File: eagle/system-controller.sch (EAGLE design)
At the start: 234 parts, among them CN1 22u, IC1 TS4100, J1 1, Q0 MOSFET-P-N-PAIR, Q1 MOSFET-P-N-PAIR, Q10 DNP/NTR4101P, Q11 DNP/NTR4101P, Q12 DNP/NTR4101P, Q13 DON3035L, Q2 MOSFET-P-N-PAIR, Q3 MOSFET-P-N-PAIR, Q4 MOSFET-P-N-PAIR, Q5 MOSFET-P-N-PAIR, Q6 MOSFET-P-N-PAIR, Q7 MOSFET-P-N-PAIR, Q9 DNP/NTR4101P, SW0 TPS25944LRVCRWQFN-20-3X4, SW1 TPS25944LRVCRWQFN-20-3X4, SW2 TPS25944LRVCRWQFN-20-3X4, SW3 TPS25944LRVCRWQFN-20-3X4, SW4 TPS25944LRVCRWQFN-20-3X4, SW5 TPS25944LRVCRWQFN-20-3X4, SW6 TPS25944LRVCRWQFN-20-3X4, SW7 TPS25944LRVCRWQFN-20-3X4, U1 MEGA128-A, X1 8 MHz CRYSTAL-ABRACON-ABM3-SMD

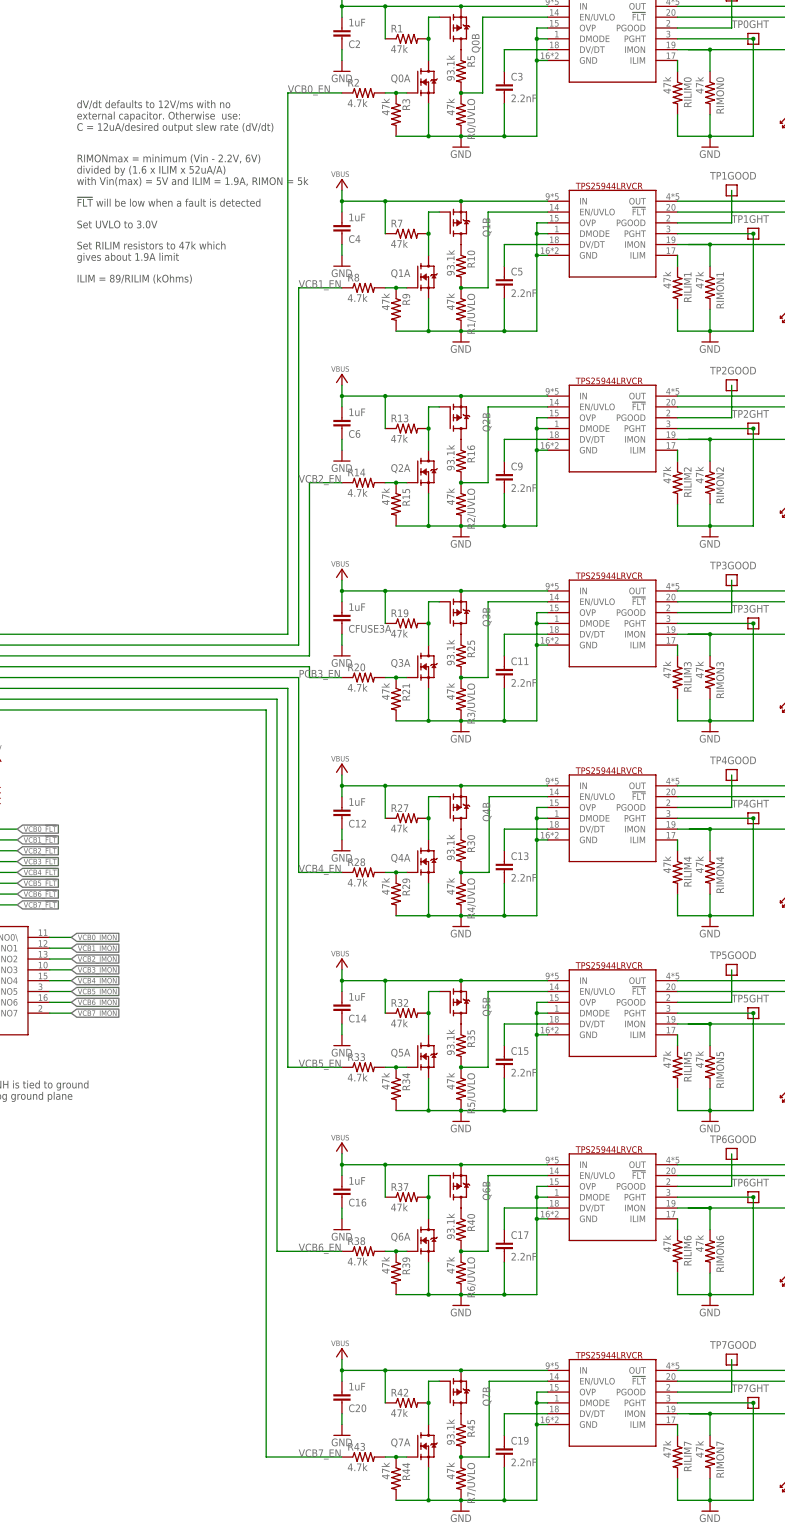
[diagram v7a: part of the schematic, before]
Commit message: made polygons wider and changed physical layout of them. Also, reduced space between traces
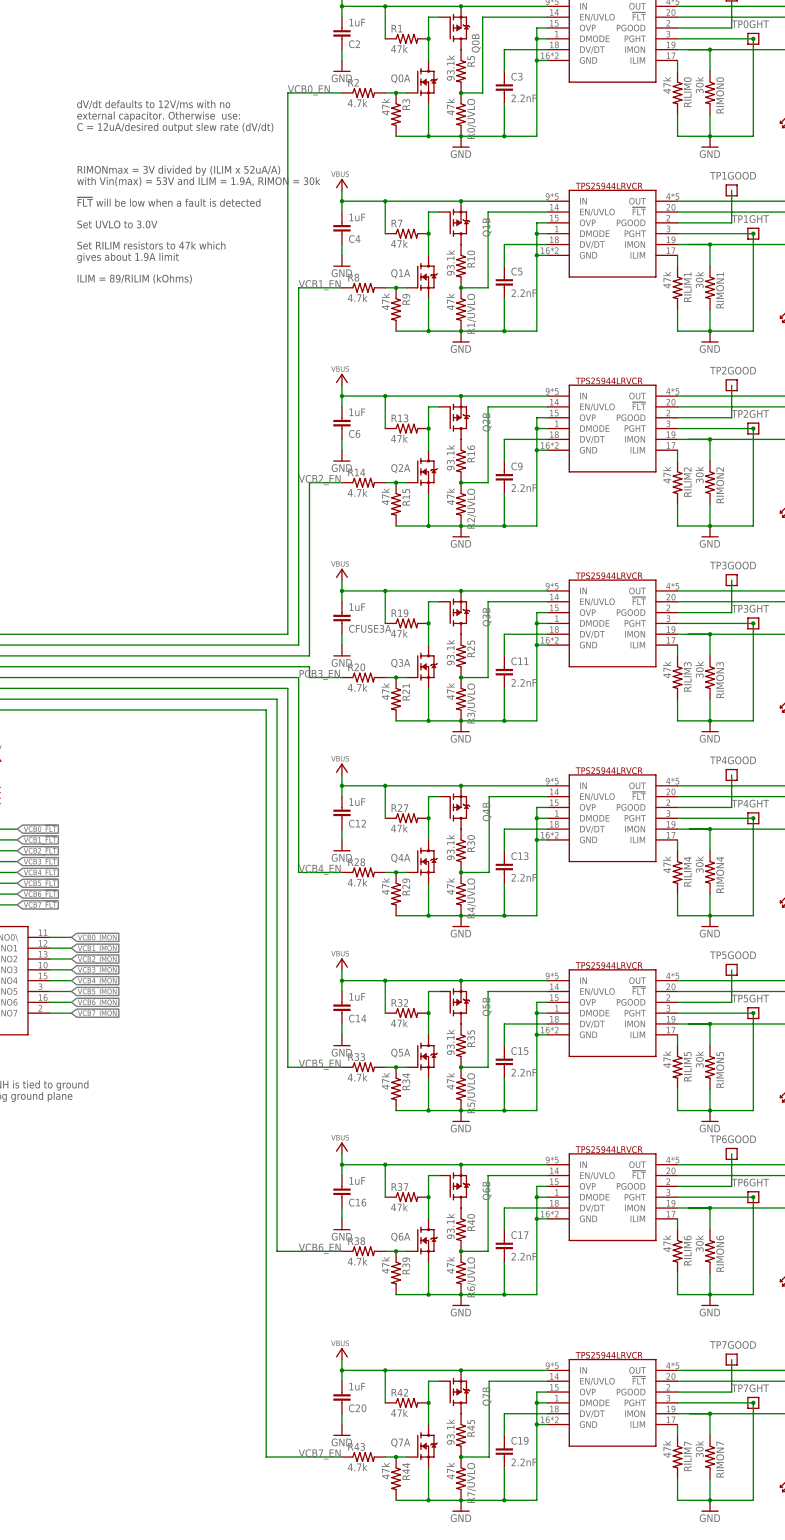
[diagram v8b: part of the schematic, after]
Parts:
- RIMON0, RIMON1, RIMON2, RIMON3, RIMON4, RIMON5, RIMON6, RIMON7: value 47k -> 30k
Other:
- note added: "RIMONmax = 3V divided by (ILIM x 52uA/A) with Vin(max) = 53V and ILIM = 1.9A, RIMON = 30k"
- note added: "To Do: Polarity chech (phoroisolator)"
- note removed: "RIMONmax = minimum (Vin - 2.2V, 6V) divided by (1.6 x ILIM x 52uA/A) with Vin(max) = 5V and ILIM = 1.9A, RIMON = 5k"
- note removed: "To Do: Look at RIMON equations Polarity chech (phoroisolator)"
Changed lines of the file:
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@@
 <attribute name="MPN" value="Texas Instruments"/>
 </part>
-<part name="RIMON0" library="rcl_custom" deviceset="R-US_" device="0603-B-NOSILK" value="47k"/>
+<part name="RIMON0" library="rcl_custom" deviceset="R-US_" device="0603-B-NOSILK" value="30k"/>
 <part name="GND" library="psas_c3_team05" deviceset="GND" device=""/>
 <part name="C3" library="rcl_custom" deviceset="C-EU" device="0603-B-NOSILK" value="2.2nF"/>
@@
 <part name="GND5" library="psas_c3_team05" deviceset="GND" device=""/>
 <part name="SW1" library="WQFN-20-3x4" deviceset="TPS25944LRVCR" device="WQFN-20-3X4"/>
-<part name="RIMON1" library="rcl_custom" deviceset="R-US_" device="0603-B-NOSILK" value="47k"/>
+<part name="RIMON1" library="rcl_custom" deviceset="R-US_" device="0603-B-NOSILK" value="30k"/>
 <part name="GND19" library="psas_c3_team05" deviceset="GND" device=""/>
 <part name="C5" library="rcl_custom" deviceset="C-EU" device="0603-B-NOSILK" value="2.2nF"/>
@@
 <part name="3V-11" library="supply-3v" deviceset="3V" device=""/>
 <part name="SW2" library="WQFN-20-3x4" deviceset="TPS25944LRVCR" device="WQFN-20-3X4"/>
-<part name="RIMON2" library="rcl_custom" deviceset="R-US_" device="0603-B-NOSILK" value="47k"/>
+<part name="RIMON2" library="rcl_custom" deviceset="R-US_" device="0603-B-NOSILK" value="30k"/>
 <part name="GND27" library="psas_c3_team05" deviceset="GND" device=""/>
 <part name="C9" library="rcl_custom" deviceset="C-EU" device="0603-B-NOSILK" value="2.2nF"/>
@@
 <part name="GND30" library="psas_c3_team05" deviceset="GND" device=""/>
 <part name="SW7" library="WQFN-20-3x4" deviceset="TPS25944LRVCR" device="WQFN-20-3X4"/>
-<part name="RIMON7" library="rcl_custom" deviceset="R-US_" device="0603-B-NOSILK" value="47k"/>
+<part name="RIMON7" library="rcl_custom" deviceset="R-US_" device="0603-B-NOSILK" value="30k"/>
 <part name="GND31" library="psas_c3_team05" deviceset="GND" device=""/>
 <part name="C19" library="rcl_custom" deviceset="C-EU" device="0603-B-NOSILK" value="2.2nF"/>
@@
 <part name="GND34" library="psas_c3_team05" deviceset="GND" device=""/>
 <part name="SW5" library="WQFN-20-3x4" deviceset="TPS25944LRVCR" device="WQFN-20-3X4"/>
-<part name="RIMON5" library="rcl_custom" deviceset="R-US_" device="0603-B-NOSILK" value="47k"/>
+<part name="RIMON5" library="rcl_custom" deviceset="R-US_" device="0603-B-NOSILK" value="30k"/>
 <part name="GND36" library="psas_c3_team05" deviceset="GND" device=""/>
 <part name="C15" library="rcl_custom" deviceset="C-EU" device="0603-B-NOSILK" value="2.2nF"/>
@@
 <part name="GND39" library="psas_c3_team05" deviceset="GND" device=""/>
 <part name="SW4" library="WQFN-20-3x4" deviceset="TPS25944LRVCR" device="WQFN-20-3X4"/>
-<part name="RIMON4" library="rcl_custom" deviceset="R-US_" device="0603-B-NOSILK" value="47k"/>
+<part name="RIMON4" library="rcl_custom" deviceset="R-US_" device="0603-B-NOSILK" value="30k"/>
 <part name="GND40" library="psas_c3_team05" deviceset="GND" device=""/>
 <part name="C13" library="rcl_custom" deviceset="C-EU" device="0603-B-NOSILK" value="2.2nF"/>
@@
 <part name="GND43" library="psas_c3_team05" deviceset="GND" device=""/>
 <part name="SW3" library="WQFN-20-3x4" deviceset="TPS25944LRVCR" device="WQFN-20-3X4"/>
-<part name="RIMON3" library="rcl_custom" deviceset="R-US_" device="0603-B-NOSILK" value="47k"/>
+<part name="RIMON3" library="rcl_custom" deviceset="R-US_" device="0603-B-NOSILK" value="30k"/>
 <part name="GND44" library="psas_c3_team05" deviceset="GND" device=""/>
 <part name="C11" library="rcl_custom" deviceset="C-EU" device="0603-B-NOSILK" value="2.2nF"/>
@@
 <part name="GND47" library="psas_c3_team05" deviceset="GND" device=""/>
 <part name="SW6" library="WQFN-20-3x4" deviceset="TPS25944LRVCR" device="WQFN-20-3X4"/>
-<part name="RIMON6" library="rcl_custom" deviceset="R-US_" device="0603-B-NOSILK" value="47k"/>
+<part name="RIMON6" library="rcl_custom" deviceset="R-US_" device="0603-B-NOSILK" value="30k"/>
 <part name="GND48" library="psas_c3_team05" deviceset="GND" device=""/>
 <part name="C17" library="rcl_custom" deviceset="C-EU" device="0603-B-NOSILK" value="2.2nF"/>
@@
 external capacitor. Otherwise  use:
 C = 12uA/desired output slew rate (dV/dt)</text>
-<text x="308.61" y="374.65" size="1.778" layer="97">RIMONmax = minimum (Vin - 2.2V, 6V)
-divided by (1.6 x ILIM x 52uA/A)
-with Vin(max) = 5V and ILIM = 1.9A, RIMON = 5k</text>
+<text x="308.61" y="374.65" size="1.778" layer="97">RIMONmax = 3V divided by (ILIM x 52uA/A)
+with Vin(max) = 53V and ILIM = 1.9A, RIMON = 30k</text>
 <text x="308.61" y="351.79" size="1.778" layer="97">ILIM = 89/RILIM (kOhms)</text>
 <text x="308.61" y="369.57" size="1.778" layer="97">!FLT! will be low when a fault is detected</text>
@@
 V_TH max = 1.4V</text>
 <text x="233.68" y="132.08" size="1.778" layer="97">P-Channel MOSFET</text>
-<text x="265.176" y="309.88" size="1.778" layer="99">To Do: Look at RIMON equations
+<text x="265.176" y="309.88" size="1.778" layer="99">To Do:
 Polarity chech (phoroisolator)</text>
 </plain>
